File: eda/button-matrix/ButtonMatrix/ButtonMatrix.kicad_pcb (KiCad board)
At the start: 2 copper layers, 87.2 x 87.2 mm, 62 parts, among them J1 Conn_01x12, J2 Conn_01x12

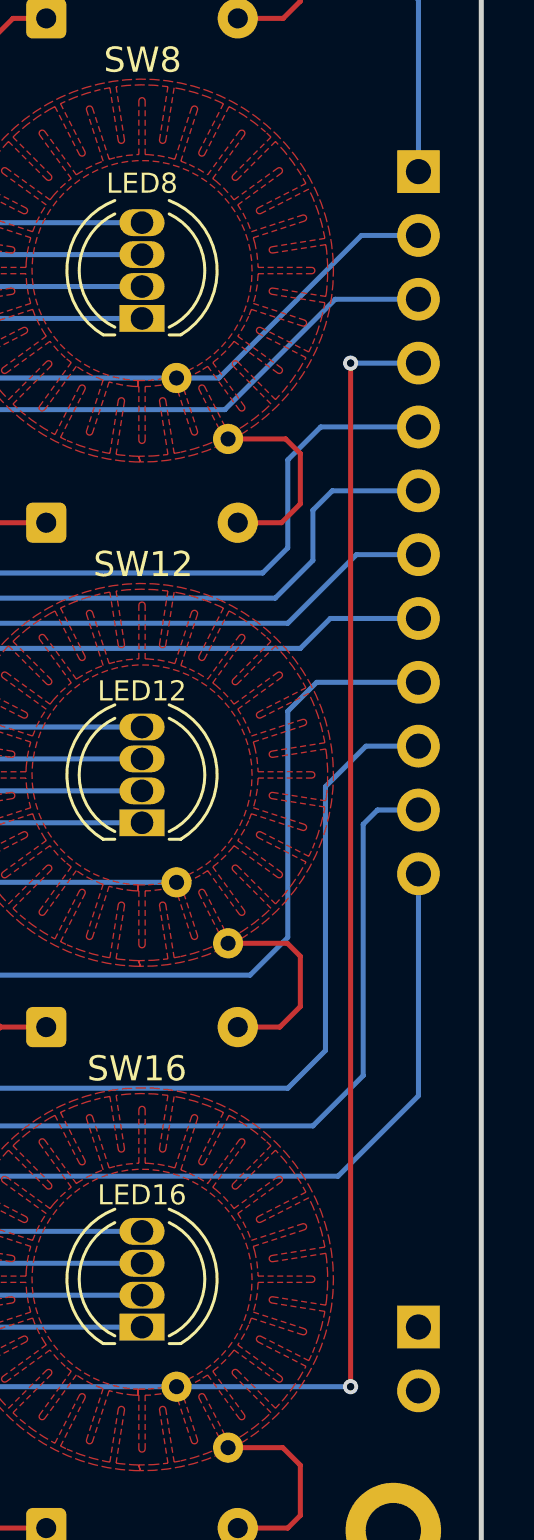
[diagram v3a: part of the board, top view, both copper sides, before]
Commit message: - Added more silkscreens to label switch headers
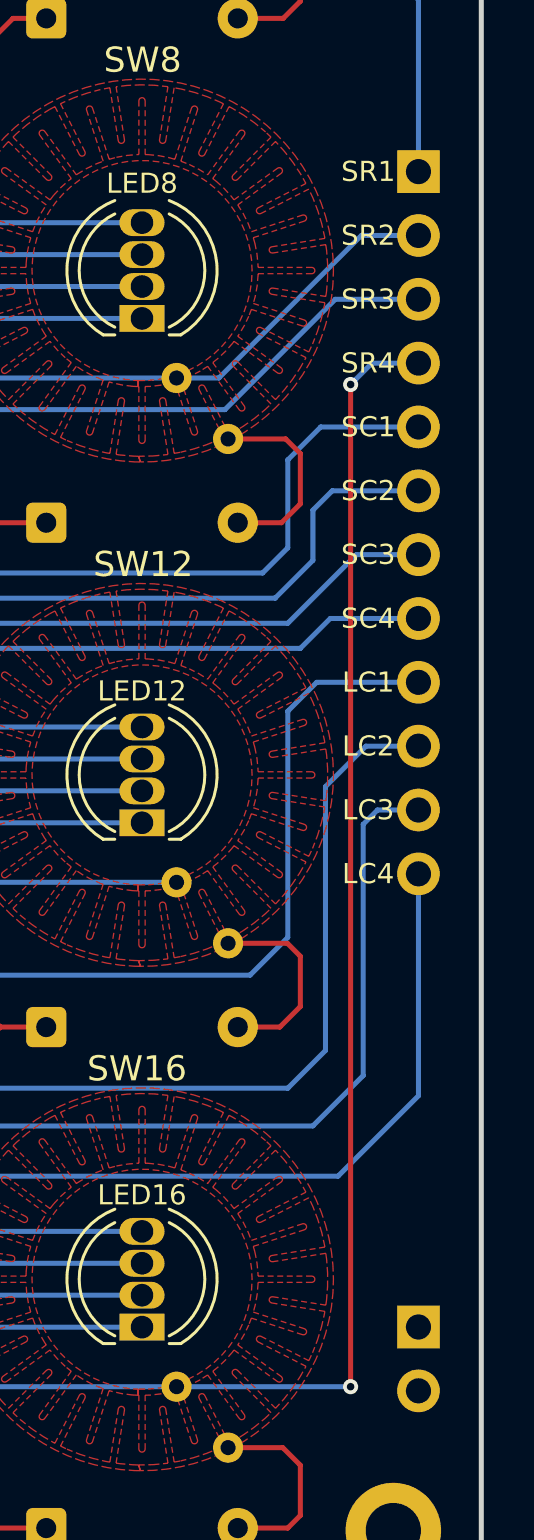
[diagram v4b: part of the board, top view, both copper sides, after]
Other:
- board text added: "LC1"
- board text added: "LC2"
- board text added: "LC3"
- board text added: "LC4"
- board text added: "SC1"
- board text added: "SC2"
- board text added: "SC3"
- board text added: "SC4"
- board text added: "SR1"
- board text added: "SR2"
- board text added: "SR3"
- board text added: "SR4"
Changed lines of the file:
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@@
 		)
 	)
+	(gr_text "SR3"
+		(at 210.7 94.11 0)
+		(layer "F.SilkS")
+		(effects
+			(font
+				(size 0.8 0.8)
+				(thickness 0.15)
+			)
+		)
+	)
 	(gr_text "R4"
 		(at 132.2 111.89 0)
@@
 		)
 	)
+	(gr_text "SC2"
+		(at 210.7 101.73 0)
+		(layer "F.SilkS")
+		(effects
+			(font
+				(size 0.8 0.8)
+				(thickness 0.15)
+			)
+		)
+	)
+	(gr_text "LC3"
+		(at 210.7 114.43 0)
+		(layer "F.SilkS")
+		(effects
+			(font
+				(size 0.8 0.8)
+				(thickness 0.15)
+			)
+		)
+	)
 	(gr_text "B1"
 		(at 132.2 94.11 0)
@@
 		)
 	)
+	(gr_text "LC4"
+		(at 210.7 116.97 0)
+		(layer "F.SilkS")
+		(effects
+			(font
+				(size 0.8 0.8)
+				(thickness 0.15)
+			)
+		)
+	)
 	(gr_text "G4"
 		(at 132.2 114.43 0)
@@
 		)
 	)
+	(gr_text "SR2"
+		(at 210.7 91.57 0)
+		(layer "F.SilkS")
+		(effects
+			(font
+				(size 0.8 0.8)
+				(thickness 0.15)
+			)
+		)
+	)
 	(gr_text "R1"
 		(at 132.2 89.03 0)
@@
 		)
 	)
+	(gr_text "SR1"
+		(at 210.7 89.03 0)
+		(layer "F.SilkS")
+		(effects
+			(font
+				(size 0.8 0.8)
+				(thickness 0.15)
+			)
+		)
+	)
+	(gr_text "SC3"
+		(at 210.7 104.27 0)
+		(layer "F.SilkS")
+		(effects
+			(font
+				(size 0.8 0.8)
+				(thickness 0.15)
+			)
+		)
+	)
+	(gr_text "SC4"
+		(at 210.7 106.81 0)
+		(layer "F.SilkS")
+		(effects
+			(font
+				(size 0.8 0.8)
+				(thickness 0.15)
+			)
+		)
+	)
 	(gr_text "B2"
 		(at 132.2 101.73 0)
@@
 		)
 	)
+	(gr_text "LC1"
+		(at 210.7 109.35 0)
+		(layer "F.SilkS")
+		(effects
+			(font
+				(size 0.8 0.8)
+				(thickness 0.15)
+			)
+		)
+	)
 	(gr_text "B4"
 		(at 132.2 116.97 0)
@@
 		)
 	)
+	(gr_text "SR4"
+		(at 210.7 96.65 0)
+		(layer "F.SilkS")
+		(effects
+			(font
+				(size 0.8 0.8)
+				(thickness 0.15)
+			)
+		)
+	)
 	(gr_text "R3"
 		(at 132.2 104.27 0)
@@
 		)
 	)
+	(gr_text "LC2"
+		(at 210.7 111.89 0)
+		(layer "F.SilkS")
+		(effects
+			(font
+				(size 0.8 0.8)
+				(thickness 0.15)
+			)
+		)
+	)
 	(gr_text "G3"
 		(at 132.2 106.81 0)
@@
 		)
 	)
+	(gr_text "SC1"
+		(at 210.7 99.19 0)
+		(layer "F.SilkS")
+		(effects
+			(font
+				(size 0.8 0.8)
+				(thickness 0.15)
+			)
+		)
+	)
 	(segment
 		(start 148 82.25)
@@
 	(segment
 		(start 210 137.375)
-		(end 210 96.65)
+		(end 210 97.5)
 		(width 0.2)
 		(layer "F.Cu")
@@
 	)
 	(via
-		(at 210 96.65)
+		(at 210 97.5)
 		(size 0.6)
 		(drill 0.3)
@@
 	)
 	(segment
+		(start 212.7 96.65)
+		(end 210.85 96.65)
+		(width 0.2)
+		(layer "B.Cu")
+		(net 24)
+	)
+	(segment
 		(start 210 137.375)
 		(end 203.075 137.375)
@@
 	)
 	(segment
-		(start 142.875 137.375)
-		(end 162.941666 137.375)
+		(start 210.85 96.65)
+		(end 210 97.5)
 		(width 0.2)
 		(layer "B.Cu")
@@
 	)
 	(segment
-		(start 212.7 96.65)
-		(end 210 96.65)
+		(start 142.875 137.375)
+		(end 162.941666 137.375)
 		(width 0.2)
 		(layer "B.Cu")
@@
 		)
 	)
+	(group ""
+		(members "0a57d325-47c8-4ccb-aba1-e7a728c85ccd" "236e80db-9d97-4aeb-8ee6-35d7ce9fd93e"
+			"466a584e-756e-48d2-9834-cefdc86fd47e" "6136bbb0-12a6-4fda-85d6-484b9f47356d"
+			"675836d3-ee7f-4e95-bd21-97d49bce727e" "7a5a9dab-2310-4176-b250-ef7f4ee9354f"
+			"8cf8a939-689a-43a9-bbec-e4c614bcfa79" "8ec5196e-15e1-4748-9970-a92a27522ce3"
+			"a86aea6a-87ab-42d5-9413-723631f73b6a" "bbcb2c23-4ef2-4786-a697-17c7312ba38f"
+			"c17967b1-3f58-48ac-a4dc-c84d0f81d5ed" "e15e953f-086e-477a-9cf1-458623f8e93c"
+		)
+	)
